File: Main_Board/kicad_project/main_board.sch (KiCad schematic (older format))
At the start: 0 parts

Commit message: add power to main board
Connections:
- net labels added: +12V, +5V
- net labels removed: +24V
- wire segments 16 -> 22

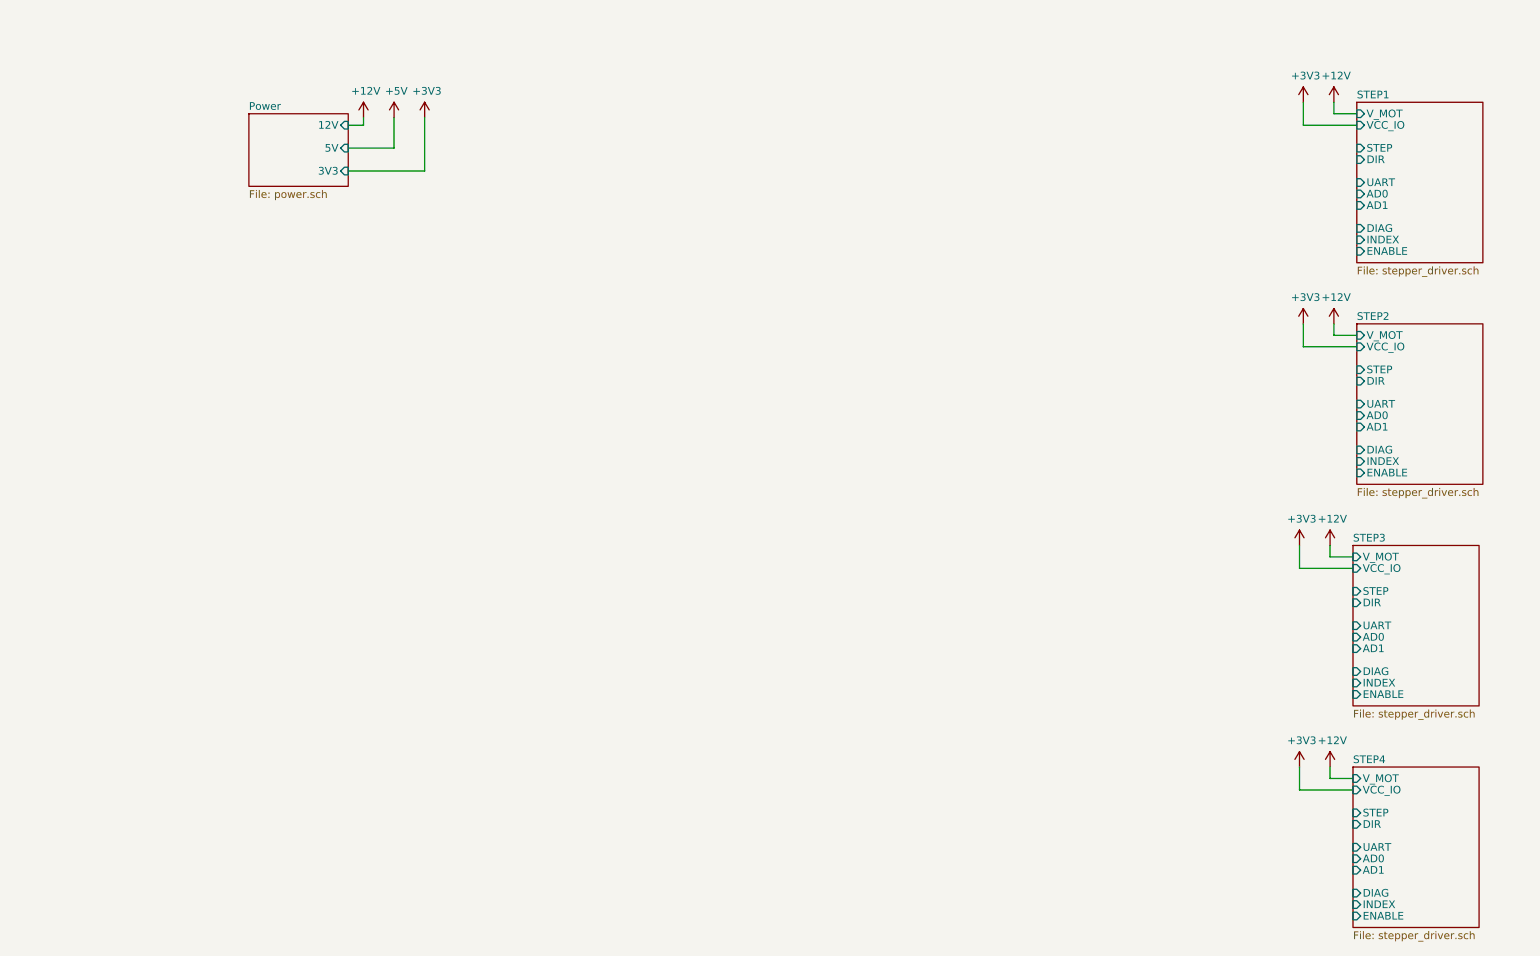
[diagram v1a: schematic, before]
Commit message: add readmes, add MCU to main board, update footprints on interface board
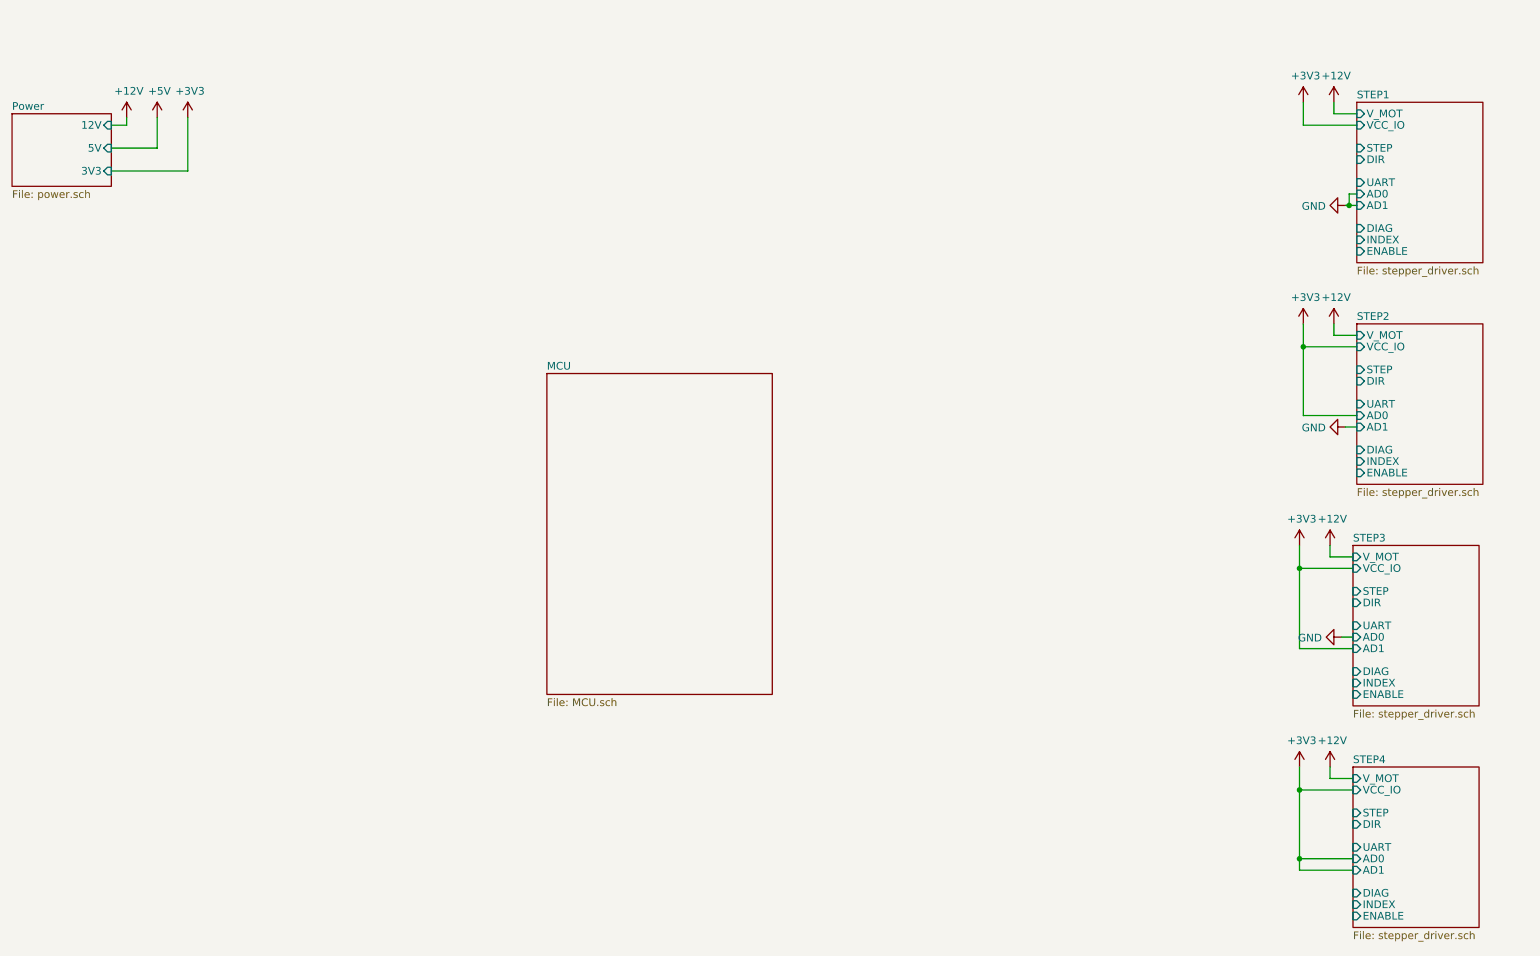
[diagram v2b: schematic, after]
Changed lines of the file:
@@
 EESchema Schematic File Version 4
-LIBS:main_board-cache
-EELAYER 29 0
+EELAYER 30 0
 EELAYER END
 $Descr A4 11693 8268
 encoding utf-8
-Sheet 1 6
+Sheet 1 7
 Title ""
 Date ""
@@
 $EndComp
 $Sheet
-S 2600 925  650  475
+S 1050 925  650  475
 U 5F4D5F3E
 F0 "Power" 50
 F1 "power.sch" 50
-F2 "3V3" I R 3250 1300 50
-F3 "12V" I R 3250 1000 50
-F4 "5V" I R 3250 1150 50
+F2 "3V3" I R 1700 1300 50
+F3 "12V" I R 1700 1000 50
+F4 "5V" I R 1700 1150 50
 $EndSheet
 $Comp
@@
 L power:+12V #PWR?
 U 1 1 5F634CDC
-P 3350 950
-F 0 "#PWR?" H 3350 800 50  0001 C CNN
-F 1 "+12V" H 3365 1123 50  0000 C CNN
-F 2 "" H 3350 950 50  0001 C CNN
-F 3 "" H 3350 950 50  0001 C CNN
-	1    3350 950
+P 1800 950
+F 0 "#PWR?" H 1800 800 50  0001 C CNN
+F 1 "+12V" H 1815 1123 50  0000 C CNN
+F 2 "" H 1800 950 50  0001 C CNN
+F 3 "" H 1800 950 50  0001 C CNN
+	1    1800 950
 	1    0    0    -1
 $EndComp
@@
 L power:+3V3 #PWR?
 U 1 1 5F635D56
-P 3750 950
-F 0 "#PWR?" H 3750 800 50  0001 C CNN
-F 1 "+3V3" H 3765 1123 50  0000 C CNN
-F 2 "" H 3750 950 50  0001 C CNN
-F 3 "" H 3750 950 50  0001 C CNN
-	1    3750 950
+P 2200 950
+F 0 "#PWR?" H 2200 800 50  0001 C CNN
+F 1 "+3V3" H 2215 1123 50  0000 C CNN
+F 2 "" H 2200 950 50  0001 C CNN
+F 3 "" H 2200 950 50  0001 C CNN
+	1    2200 950
 	1    0    0    -1
 $EndComp
@@
 L power:+5V #PWR?
 U 1 1 5F636812
-P 3550 950
-F 0 "#PWR?" H 3550 800 50  0001 C CNN
-F 1 "+5V" H 3565 1123 50  0000 C CNN
-F 2 "" H 3550 950 50  0001 C CNN
-F 3 "" H 3550 950 50  0001 C CNN
-	1    3550 950
-	1    0    0    -1
-$EndComp
-Wire Wire Line
-	3750 950  3750 1300
-Wire Wire Line
-	3750 1300 3250 1300
-Wire Wire Line
-	3250 1150 3550 1150
-Wire Wire Line
-	3550 1150 3550 950
-Wire Wire Line
-	3250 1000 3350 1000
-Wire Wire Line
-	3350 1000 3350 950
+P 2000 950
+F 0 "#PWR?" H 2000 800 50  0001 C CNN
+F 1 "+5V" H 2015 1123 50  0000 C CNN
+F 2 "" H 2000 950 50  0001 C CNN
+F 3 "" H 2000 950 50  0001 C CNN
+	1    2000 950
+	1    0    0    -1
+$EndComp
+Wire Wire Line
+	2200 950  2200 1300
+Wire Wire Line
+	2200 1300 1700 1300
+Wire Wire Line
+	1700 1150 2000 1150
+Wire Wire Line
+	2000 1150 2000 950
+Wire Wire Line
+	1700 1000 1800 1000
+Wire Wire Line
+	1800 1000 1800 950
+Wire Wire Line
+	9825 4425 9475 4425
+Wire Wire Line
+	9475 4425 9475 3900
+Connection ~ 9475 3900
+Wire Wire Line
+	9825 5800 9475 5800
+Wire Wire Line
+	9475 5800 9475 5350
+Connection ~ 9475 5350
+Wire Wire Line
+	9825 5875 9475 5875
+Wire Wire Line
+	9475 5875 9475 5800
+Connection ~ 9475 5800
+$Comp
+L power:GND #PWR?
+U 1 1 5F537589
+P 9775 1525
+F 0 "#PWR?" H 9775 1275 50  0001 C CNN
+F 1 "GND" V 9780 1397 50  0000 R CNN
+F 2 "" H 9775 1525 50  0001 C CNN
+F 3 "" H 9775 1525 50  0001 C CNN
+	1    9775 1525
+	0    1    1    0
+$EndComp
+$Comp
+L power:GND #PWR?
+U 1 1 5F53878C
+P 9775 2975
+F 0 "#PWR?" H 9775 2725 50  0001 C CNN
+F 1 "GND" V 9780 2847 50  0000 R CNN
+F 2 "" H 9775 2975 50  0001 C CNN
+F 3 "" H 9775 2975 50  0001 C CNN
+	1    9775 2975
+	0    1    1    0
+$EndComp
+Wire Wire Line
+	9750 4350 9825 4350
+Wire Wire Line
+	9775 2975 9850 2975
+Wire Wire Line
+	9775 1525 9800 1525
+Wire Wire Line
+	9850 1450 9800 1450
+Wire Wire Line
+	9800 1450 9800 1525
+Connection ~ 9800 1525
+Wire Wire Line
+	9800 1525 9850 1525
+Wire Wire Line
+	9850 2900 9500 2900
+Connection ~ 9500 2450
+Wire Wire Line
+	9500 2900 9500 2450
+$Comp
+L power:GND #PWR?
+U 1 1 5F5393A9
+P 9750 4350
+F 0 "#PWR?" H 9750 4100 50  0001 C CNN
+F 1 "GND" V 9755 4222 50  0000 R CNN
+F 2 "" H 9750 4350 50  0001 C CNN
+F 3 "" H 9750 4350 50  0001 C CNN
+	1    9750 4350
+	0    1    1    0
+$EndComp
+$Sheet
+S 4550 2625 1475 2100
+U 5F5463C2
+F0 "MCU" 50
+F1 "MCU.sch" 50
+$EndSheet
 $EndSCHEMATC

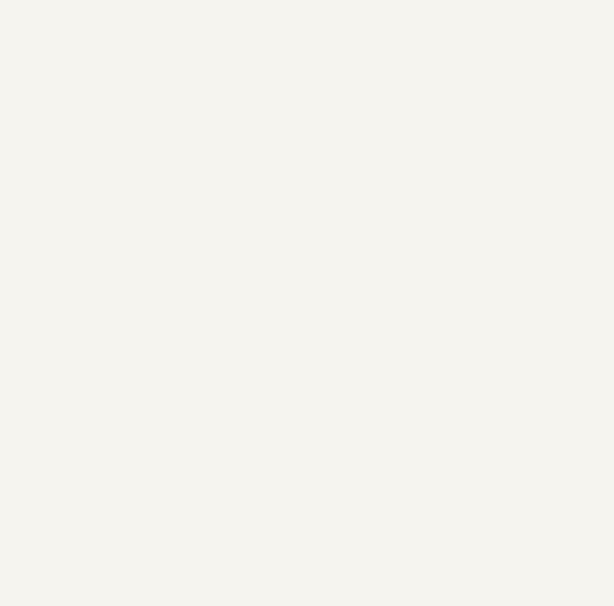
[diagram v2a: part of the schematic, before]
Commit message: add input/output schematic, add documentation
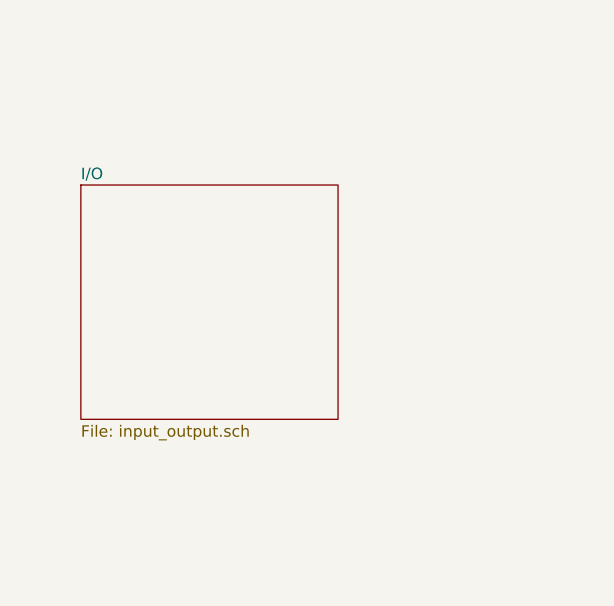
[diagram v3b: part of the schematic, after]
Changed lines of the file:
@@
 $Descr A4 11693 8268
 encoding utf-8
-Sheet 1 7
-Title ""
+Sheet 1 8
+Title "Cube Main Board - top level schematic"
 Date ""
 Rev ""
-Comp ""
-Comment1 ""
+Comp "Oldřich Pecák (LoaDy)"
+Comment1 "Preliminary license: CERN OHWL-P v2 ?"
 Comment2 ""
 Comment3 ""
@@
 F1 "MCU.sch" 50
 $EndSheet
+$Sheet
+S 1325 2775 1125 1025
+U 5F51A37F
+F0 "I/O" 50
+F1 "input_output.sch" 50
+$EndSheet
 $EndSCHEMATC

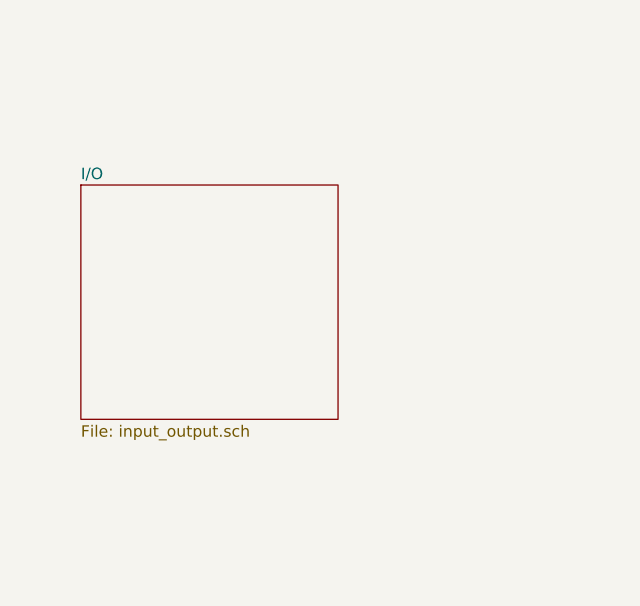
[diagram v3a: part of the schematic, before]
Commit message: Fix I/O protection
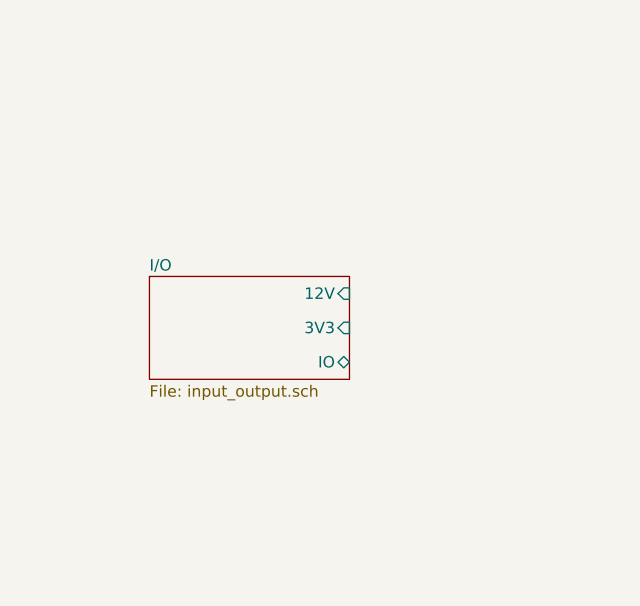
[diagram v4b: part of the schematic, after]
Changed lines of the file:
@@
 $EndSheet
 $Sheet
-S 1325 2775 1125 1025
+S 1625 3175 875  450
 U 5F51A37F
 F0 "I/O" 50
 F1 "input_output.sch" 50
+F2 "3V3" I R 2500 3400 50
+F3 "12V" I R 2500 3250 50
+F4 "IO" B R 2500 3550 50
 $EndSheet
 $EndSCHEMATC
